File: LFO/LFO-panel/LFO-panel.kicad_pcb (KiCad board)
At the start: 2 copper layers, 30 x 128.5 mm, 0 parts

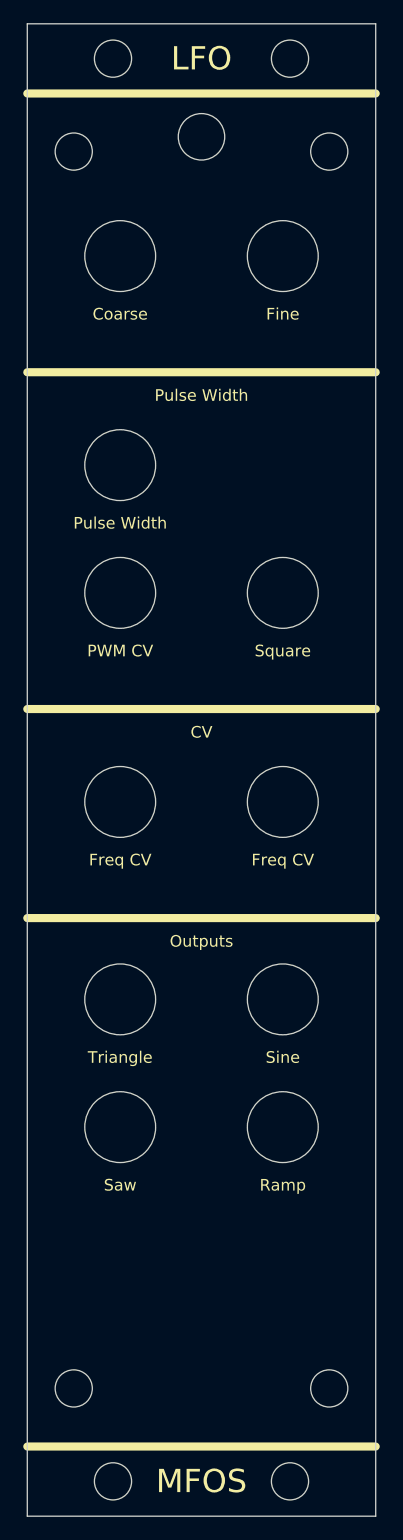
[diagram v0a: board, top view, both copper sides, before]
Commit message: minor cleanup of silkscreen
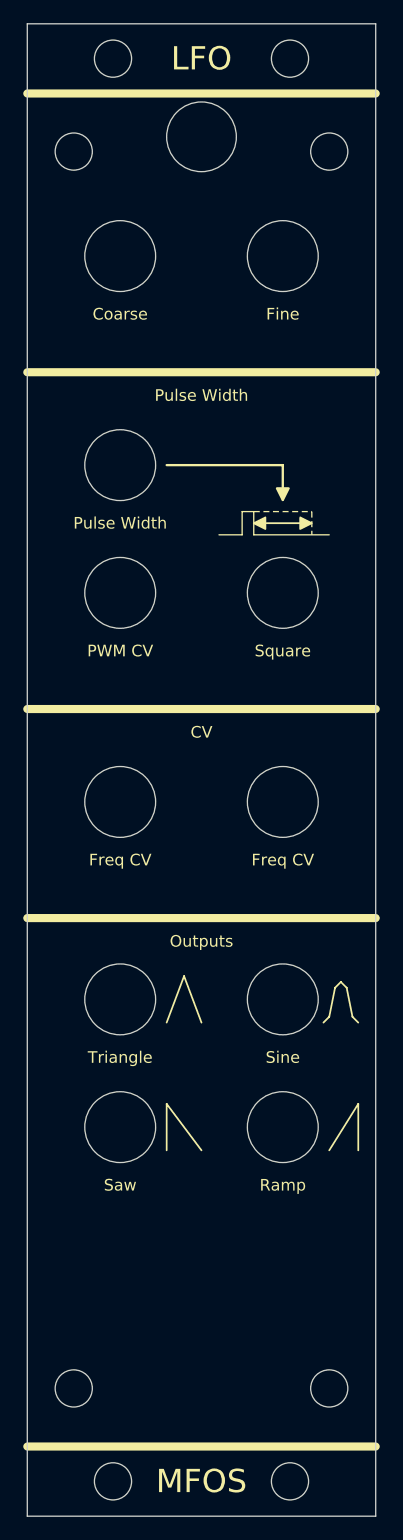
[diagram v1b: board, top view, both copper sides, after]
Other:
- outline, holes or cut-outs redrawn
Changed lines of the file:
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@@
   )
   (net 0 "")
+  (gr_line (start 19.5 42) (end 19.5 44)
+    (stroke (width 0.1) (type default)) (layer "F.SilkS"))
+  (gr_line (start 27.5 83) (end 27 82.5)
+    (stroke (width 0.15) (type default)) (layer "F.SilkS"))
+  (gr_line (start 18.5 44) (end 18.5 42)
+    (stroke (width 0.1) (type default)) (layer "F.SilkS"))
+  (gr_line (start 26 85.5) (end 26.5 83)
+    (stroke (width 0.15) (type default)) (layer "F.SilkS"))
+  (gr_line (start 26.5 83) (end 27 82.5)
+    (stroke (width 0.15) (type default)) (layer "F.SilkS"))
   (gr_line (start 0 122.5) (end 30 122.5)
     (stroke (width 0.7) (type default)) (layer "F.SilkS"))
+  (gr_poly
+    (pts
+      (xy 19.5 43)
+      (xy 20.5 42.5)
+      (xy 20.5 43.5)
+    )
+    (stroke (width 0.15) (type solid)) (fill solid) (layer "F.SilkS"))
   (gr_line (start 0 77) (end 30 77)
     (stroke (width 0.7) (type default)) (layer "F.SilkS"))
   (gr_line (start 0 59) (end 30 59)
     (stroke (width 0.7) (type default)) (layer "F.SilkS"))
+  (gr_line (start 19.5 44) (end 26 44)
+    (stroke (width 0.1) (type default)) (layer "F.SilkS"))
+  (gr_line (start 24.5 42) (end 24.5 44)
+    (stroke (width 0.1) (type dot)) (layer "F.SilkS"))
+  (gr_poly
+    (pts
+      (xy 24.5 43)
+      (xy 23.5 42.5)
+      (xy 23.5 43.5)
+    )
+    (stroke (width 0.15) (type solid)) (fill solid) (layer "F.SilkS"))
+  (gr_line (start 25.5 86) (end 26 85.5)
+    (stroke (width 0.15) (type default)) (layer "F.SilkS"))
+  (gr_line (start 12 97) (end 12 93)
+    (stroke (width 0.15) (type default)) (layer "F.SilkS"))
+  (gr_line (start 12 38) (end 22 38)
+    (stroke (width 0.2) (type default)) (layer "F.SilkS"))
+  (gr_poly
+    (pts
+      (xy 22 41)
+      (xy 21.5 40)
+      (xy 22.5 40)
+    )
+    (stroke (width 0.2) (type solid)) (fill solid) (layer "F.SilkS"))
+  (gr_line (start 28.5 86) (end 28 85.5)
+    (stroke (width 0.15) (type default)) (layer "F.SilkS"))
+  (gr_line (start 16.5 44) (end 18.5 44)
+    (stroke (width 0.1) (type default)) (layer "F.SilkS"))
+  (gr_line (start 19.5 42) (end 24.5 42)
+    (stroke (width 0.1) (type dot)) (layer "F.SilkS"))
+  (gr_line (start 12 86) (end 13.5 82)
+    (stroke (width 0.15) (type default)) (layer "F.SilkS"))
   (gr_line (start 0 30) (end 30 30)
     (stroke (width 0.7) (type default)) (layer "F.SilkS"))
+  (gr_line (start 28 85.5) (end 27.5 83)
+    (stroke (width 0.15) (type default)) (layer "F.SilkS"))
+  (gr_line (start 22 38) (end 22 41)
+    (stroke (width 0.2) (type default)) (layer "F.SilkS"))
+  (gr_line (start 13.5 82) (end 15 86)
+    (stroke (width 0.15) (type default)) (layer "F.SilkS"))
+  (gr_line (start 20 43) (end 24 43)
+    (stroke (width 0.15) (type default)) (layer "F.SilkS"))
   (gr_line (start 0 6) (end 30 6)
     (stroke (width 0.7) (type default)) (layer "F.SilkS"))
+  (gr_line (start 26 97) (end 28.5 93)
+    (stroke (width 0.15) (type default)) (layer "F.SilkS"))
+  (gr_line (start 28.5 93) (end 28.5 97)
+    (stroke (width 0.15) (type default)) (layer "F.SilkS"))
+  (gr_line (start 12 93) (end 15 97)
+    (stroke (width 0.15) (type default)) (layer "F.SilkS"))
+  (gr_line (start 18.5 42) (end 19.5 42)
+    (stroke (width 0.1) (type default)) (layer "F.SilkS"))
   (gr_circle (center 8 38) (end 11.05 38)
     (stroke (width 0.1) (type default)) (fill none) (layer "Edge.Cuts"))
@@
   (gr_circle (center 22 84) (end 25.05 84)
     (stroke (width 0.1) (type default)) (fill none) (layer "Edge.Cuts"))
-  (gr_circle (center 15 9.73) (end 17 9.73)
+  (gr_circle (center 15 9.73) (end 18 9.73)
     (stroke (width 0.1) (type default)) (fill none) (layer "Edge.Cuts"))
   (gr_circle (center 7.38 125.5) (end 8.98 125.5)
